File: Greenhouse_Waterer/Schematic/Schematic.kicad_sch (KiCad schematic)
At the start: 16 parts, among them J1 12V in, J2 Pump Control, J3 Pump Control, M1 Pump Motor, P1 Conn_Plug_3P_Protected, SW1 ON/OFF, U2 PCF8575DBR, U3 WEMOS_D1_mini, U4 HHG1D-1

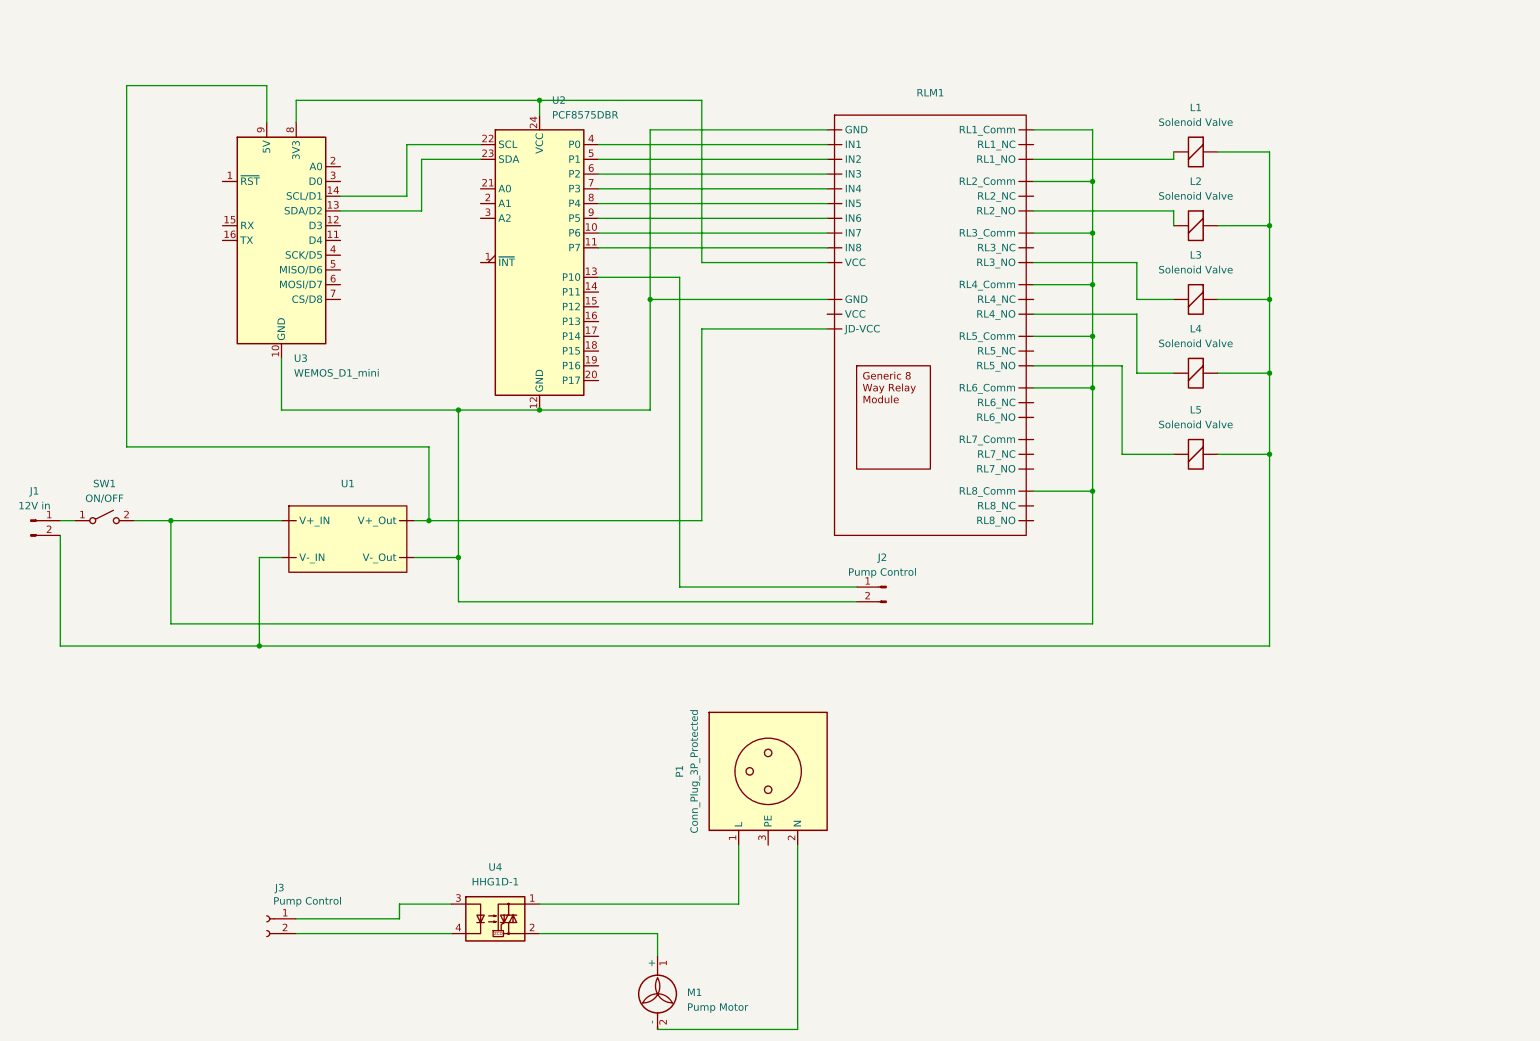
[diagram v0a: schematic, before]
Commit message: Added water butt level transmitter.  Updated schematic for as-built condition (as of 18/06/2025)
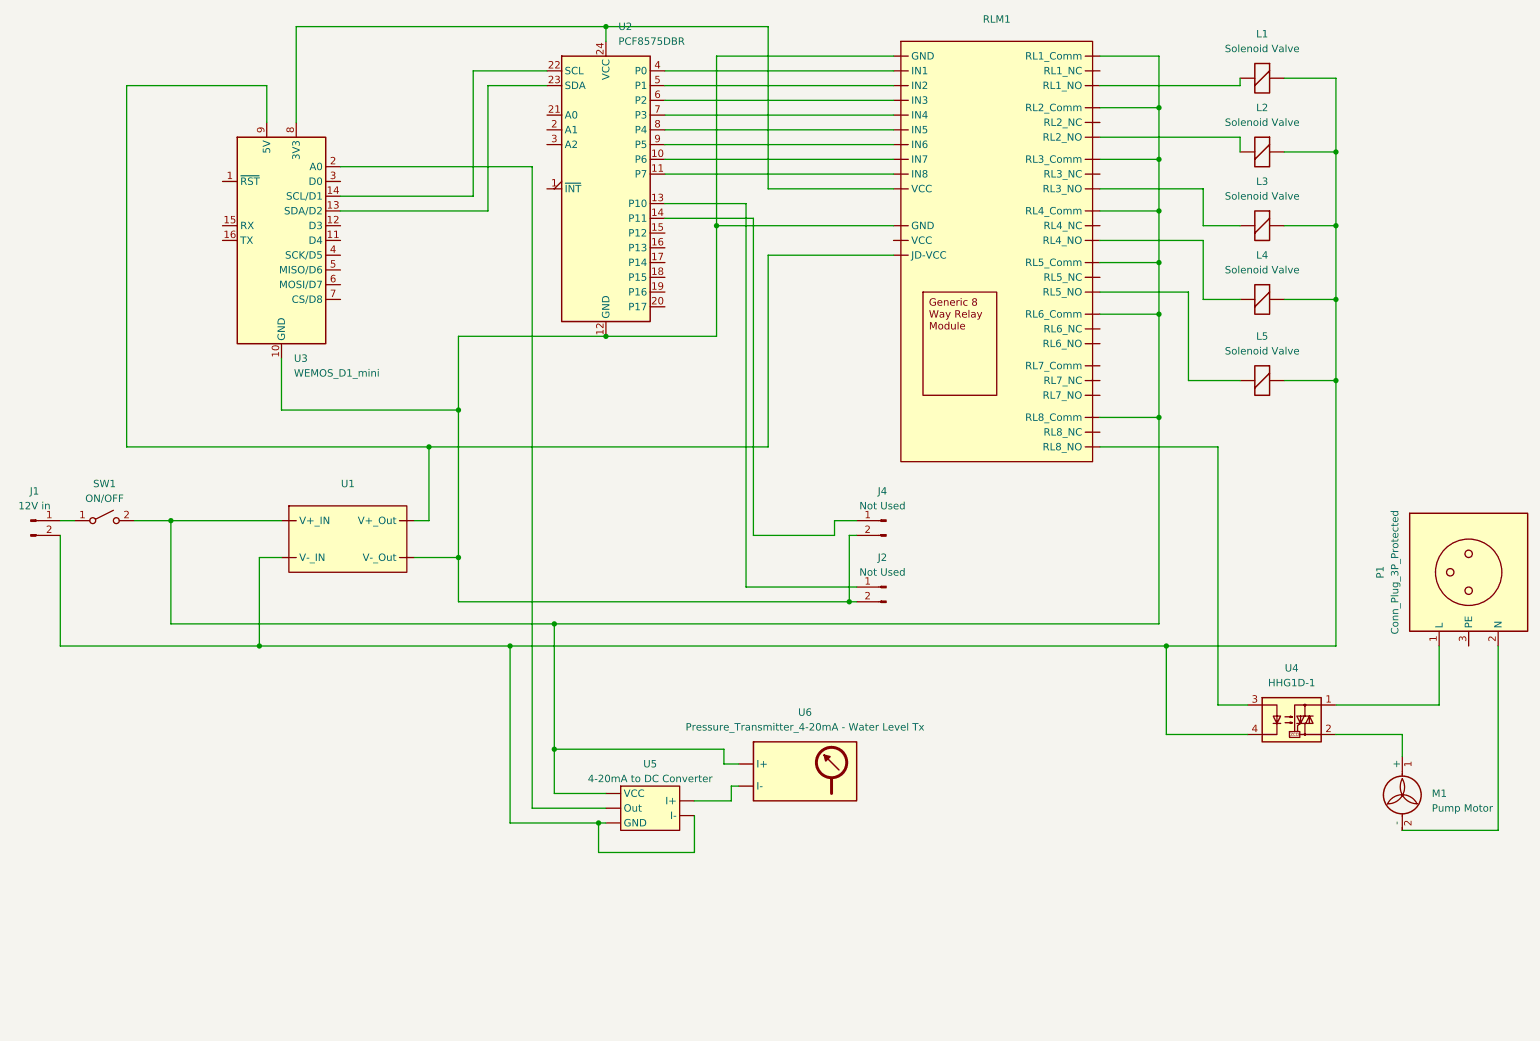
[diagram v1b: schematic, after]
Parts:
- removed J3: Pump Control, symbol Connector:Conn_01x02_Socket
- added J4: Not Used, symbol Connector:Conn_01x02_Pin
- added U5: 4-20mA to DC Converter, symbol Modules:4-20mA_to_DC
- added U6: Pressure_Transmitter_4-20mA - Water Level Tx, symbol Modules:Pressure_Transmitter_4-20mA
- J2: value Pump Control -> Not Used
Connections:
- net at J1.2 (Pin_2), L1.1 (-), L2.1 (-)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: now also U4.4, U5. (I-)
- net at J2.2 (Pin_2), RLM1. (RL8_NO), U1. (V-_Out)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: now also J4.2 (Pin_2)
- net at U4.3: now also RLM1. (RL8_NO)
- net at RLM1. (RL8_NO): now also L5.2 (+)
- net at U3.2 (A0): now also U5. (I-)
- net at U2.14 (P11): now also J4.1 (Pin_1)
- new net: RLM1. (RL8_NO), SW1.2 (B), U1. (V-_Out), U5. (I-), U6. (I-)
- new net: U5. (I-), U6. (I-)
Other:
- company: (none) -> GJ
- title: (none) -> Greenhouse Waterer
- moved on the sheet: L1, L2, L3, L4, L5, M1, P1, U2, U4
